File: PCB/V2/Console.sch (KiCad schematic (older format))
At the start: 11 parts

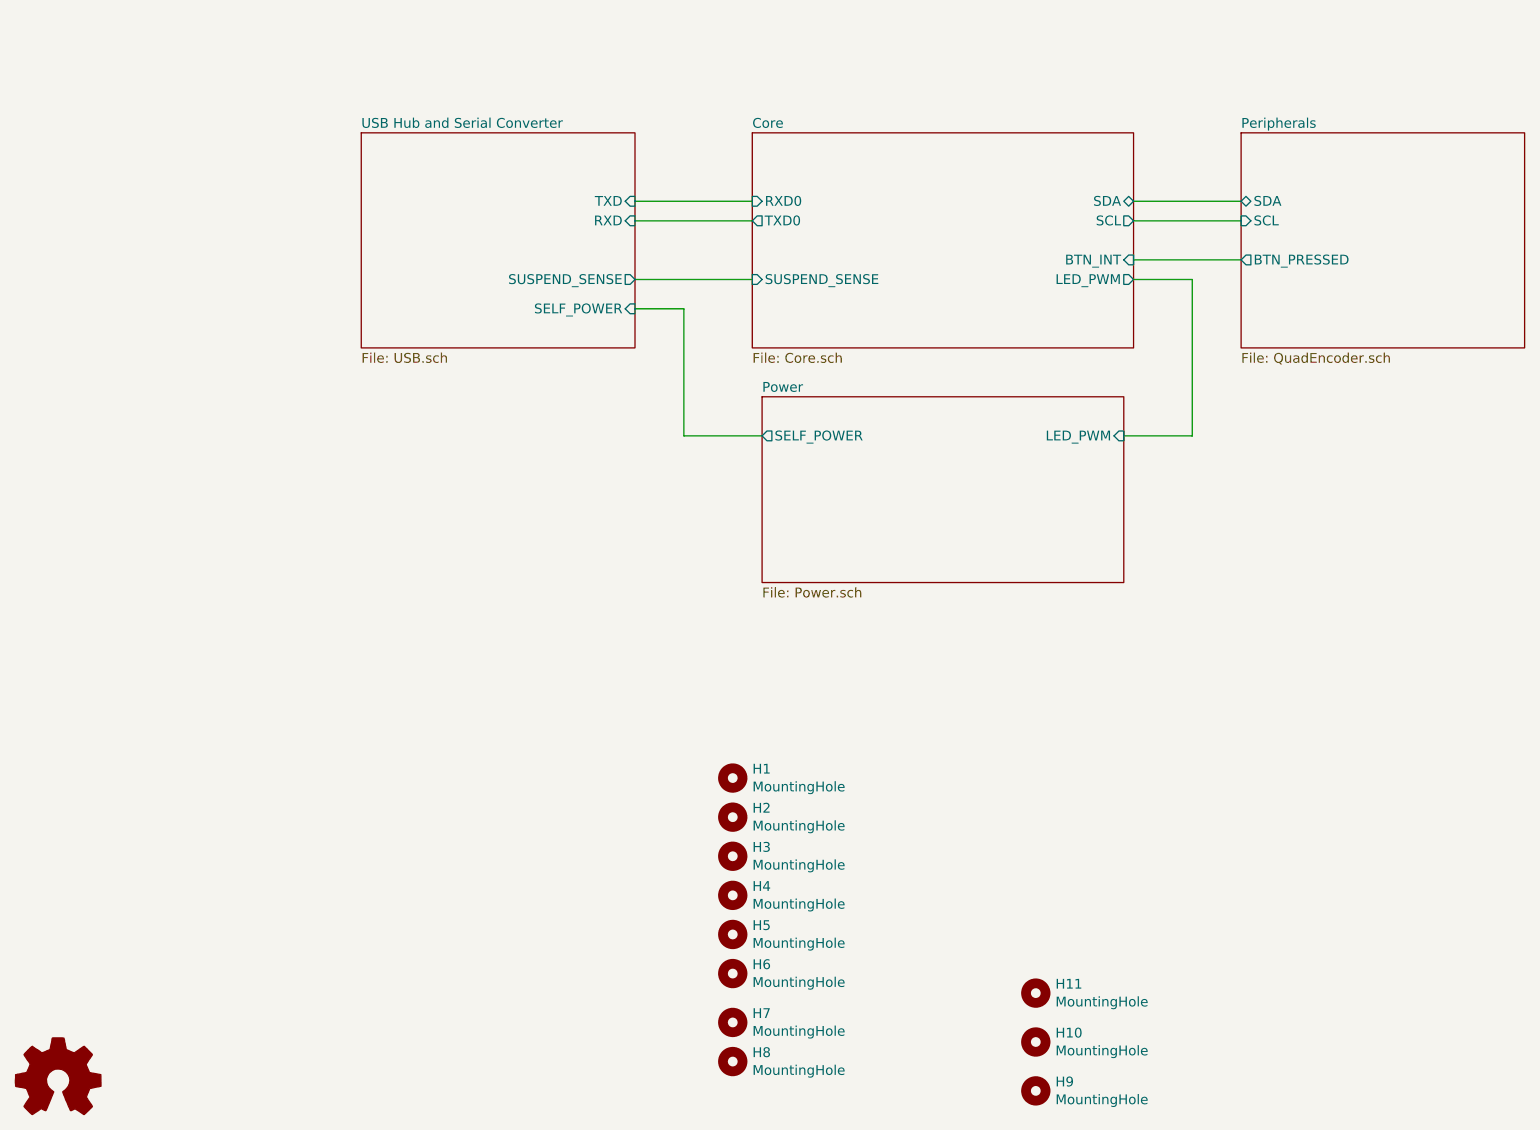
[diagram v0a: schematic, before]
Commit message: WIP schematic work, ready to route board V2
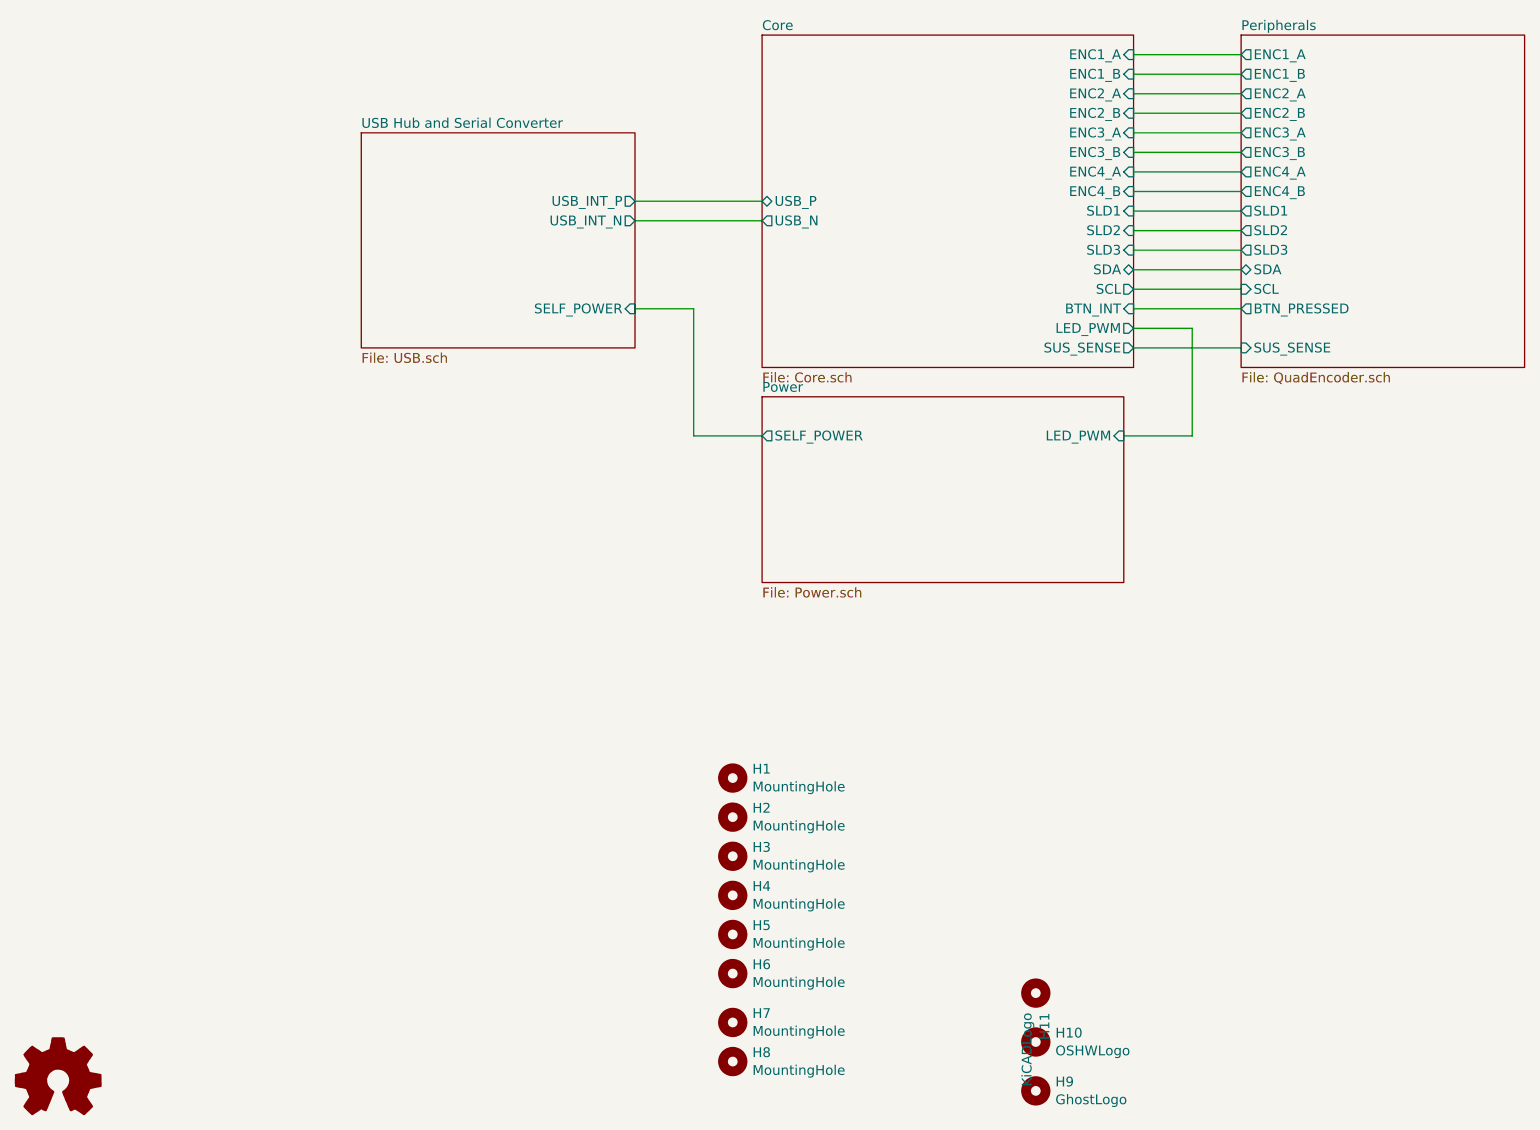
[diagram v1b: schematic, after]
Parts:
- H10: value MountingHole -> OSHWLogo
- H11: value MountingHole -> KiCADLogo
- H9: value MountingHole -> GhostLogo
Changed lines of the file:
@@
 $EndDescr
 $Sheet
-S 6850 2850 1450 1100
+S 6850 2350 1450 1700
 U 5F4A9E86
 F0 "Peripherals" 50
 F1 "QuadEncoder.sch" 50
-F2 "SCL" I L 6850 3300 50
-F3 "SDA" B L 6850 3200 50
-F4 "BTN_PRESSED" O L 6850 3500 50
+F2 "SCL" I L 6850 3650 50
+F3 "SDA" B L 6850 3550 50
+F4 "BTN_PRESSED" O L 6850 3750 50
+F5 "ENC1_A" O L 6850 2450 50
+F6 "ENC1_B" O L 6850 2550 50
+F7 "ENC2_A" O L 6850 2650 50
+F8 "ENC2_B" O L 6850 2750 50
+F9 "ENC3_A" O L 6850 2850 50
+F10 "ENC3_B" O L 6850 2950 50
+F11 "ENC4_A" O L 6850 3050 50
+F12 "ENC4_B" O L 6850 3150 50
+F13 "SLD1" O L 6850 3250 50
+F14 "SLD2" O L 6850 3350 50
+F15 "SLD3" O L 6850 3450 50
+F16 "SUS_SENSE" I L 6850 3950 50
 $EndSheet
 $Sheet
@@
 F1 "USB.sch" 50
 F2 "SELF_POWER" I R 3750 3750 50
-F3 "TXD" I R 3750 3200 50
-F4 "RXD" I R 3750 3300 50
-F5 "SUSPEND_SENSE" O R 3750 3600 50
-$EndSheet
-Wire Wire Line
-	3750 3200 4350 3200
-Wire Wire Line
-	4350 3300 3750 3300
-Wire Wire Line
-	3750 3600 4350 3600
-Wire Wire Line
-	6300 3200 6850 3200
-Wire Wire Line
-	6300 3300 6850 3300
-Wire Wire Line
-	6300 3500 6850 3500
+F3 "USB_INT_P" O R 3750 3200 50
+F4 "USB_INT_N" O R 3750 3300 50
+$EndSheet
 $Sheet
 S 4400 4200 1850 950
@@
 $EndSheet
 Wire Wire Line
-	4000 3750 3750 3750
+	4050 3750 3750 3750
 Wire Wire Line
 	6250 4400 6600 4400
 Wire Wire Line
-	6600 4400 6600 3600
-Wire Wire Line
-	6600 3600 6300 3600
-Wire Wire Line
-	4000 4400 4000 3750
-Wire Wire Line
-	4400 4400 4000 4400
-$Sheet
-S 4350 2850 1950 1100
-U 5F4A9D3D
-F0 "Core" 50
-F1 "Core.sch" 50
-F2 "SDA" B R 6300 3200 50
-F3 "TXD0" O L 4350 3300 50
-F4 "RXD0" I L 4350 3200 50
-F5 "SCL" O R 6300 3300 50
-F6 "SUSPEND_SENSE" I L 4350 3600 50
-F7 "BTN_INT" I R 6300 3500 50
-F8 "LED_PWM" O R 6300 3600 50
-$EndSheet
+	6600 4400 6600 3850
+Wire Wire Line
+	6600 3850 6300 3850
+Wire Wire Line
+	4050 4400 4050 3750
+Wire Wire Line
+	4400 4400 4050 4400
 $Comp
 L Mechanical:MountingHole H1
@@
 P 5800 7750
 F 0 "H9" H 5900 7796 50  0000 L CNN
-F 1 "MountingHole" H 5900 7705 50  0000 L CNN
+F 1 "GhostLogo" H 5900 7705 50  0000 L CNN
 F 2 "EMRSNxEOS:Ghost" H 5800 7750 50  0001 C CNN
 F 3 "~" H 5800 7750 50  0001 C CNN
@@
 P 5800 7500
 F 0 "H10" H 5900 7546 50  0000 L CNN
-F 1 "MountingHole" H 5900 7455 50  0000 L CNN
+F 1 "OSHWLogo" H 5900 7455 50  0000 L CNN
 F 2 "Symbol:OSHW-Logo_5.7x6mm_SilkScreen" H 5800 7500 50  0001 C CNN
 F 3 "~" H 5800 7500 50  0001 C CNN
@@
 P 5800 7250
 F 0 "H11" H 5900 7296 50  0000 L CNN
-F 1 "MountingHole" H 5900 7205 50  0000 L CNN
+F 1 "KiCADLogo" H 5900 7205 50  0000 L CNN
 F 2 "Symbol:KiCad-Logo2_5mm_SilkScreen" H 5800 7250 50  0001 C CNN
 F 3 "~" H 5800 7250 50  0001 C CNN
 	1    5800 7250
-	1    0    0    -1
-$EndComp
+	0    1    1    0
+$EndComp
+Wire Wire Line
+	3750 3200 4400 3200
+Wire Wire Line
+	4400 3300 3750 3300
+Wire Wire Line
+	6850 3550 6300 3550
+Wire Wire Line
+	6300 3650 6850 3650
+Wire Wire Line
+	6850 3750 6300 3750
+$Sheet
+S 4400 2350 1900 1700
+U 5F4A9D3D
+F0 "Core" 50
+F1 "Core.sch" 50
+F2 "SDA" B R 6300 3550 50
+F3 "SCL" O R 6300 3650 50
+F4 "BTN_INT" I R 6300 3750 50
+F5 "LED_PWM" O R 6300 3850 50
+F6 "SLD3" I R 6300 3450 50
+F7 "SLD2" I R 6300 3350 50
+F8 "SLD1" I R 6300 3250 50
+F9 "ENC4_B" I R 6300 3150 50
+F10 "ENC4_A" I R 6300 3050 50
+F11 "ENC3_B" I R 6300 2950 50
+F12 "ENC3_A" I R 6300 2850 50
+F13 "ENC2_B" I R 6300 2750 50
+F14 "ENC2_A" I R 6300 2650 50
+F15 "ENC1_B" I R 6300 2550 50
+F16 "ENC1_A" I R 6300 2450 50
+F17 "USB_N" O L 4400 3300 50
+F18 "USB_P" B L 4400 3200 50
+F19 "SUS_SENSE" O R 6300 3950 50
+$EndSheet
+Wire Wire Line
+	6300 3450 6850 3450
+Wire Wire Line
+	6850 3350 6300 3350
+Wire Wire Line
+	6300 3250 6850 3250
+Wire Wire Line
+	6850 3150 6300 3150
+Wire Wire Line
+	6300 3050 6850 3050
+Wire Wire Line
+	6850 2950 6300 2950
+Wire Wire Line
+	6300 2850 6850 2850
+Wire Wire Line
+	6850 2750 6300 2750
+Wire Wire Line
+	6300 2650 6850 2650
+Wire Wire Line
+	6850 2550 6300 2550
+Wire Wire Line
+	6300 2450 6850 2450
+Wire Wire Line
+	6850 3950 6300 3950
 $EndSCHEMATC
